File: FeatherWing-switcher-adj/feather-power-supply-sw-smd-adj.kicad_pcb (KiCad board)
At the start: 2 copper layers, 20 parts, among them J2 Conn_01x16, J3 QWIIC, J4 0.1, Q1 Q_PMOS_GSD, U1 MCP16312MS

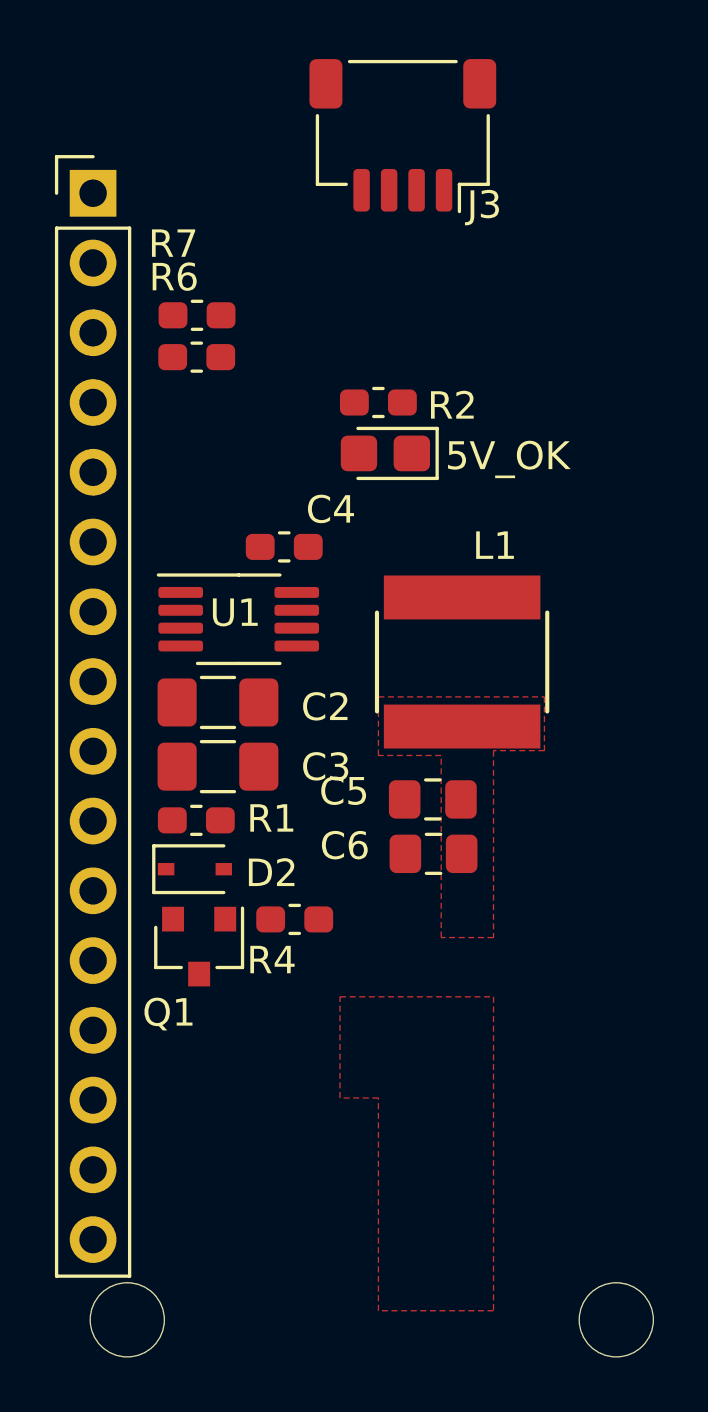
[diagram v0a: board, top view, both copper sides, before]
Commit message: adds input switch
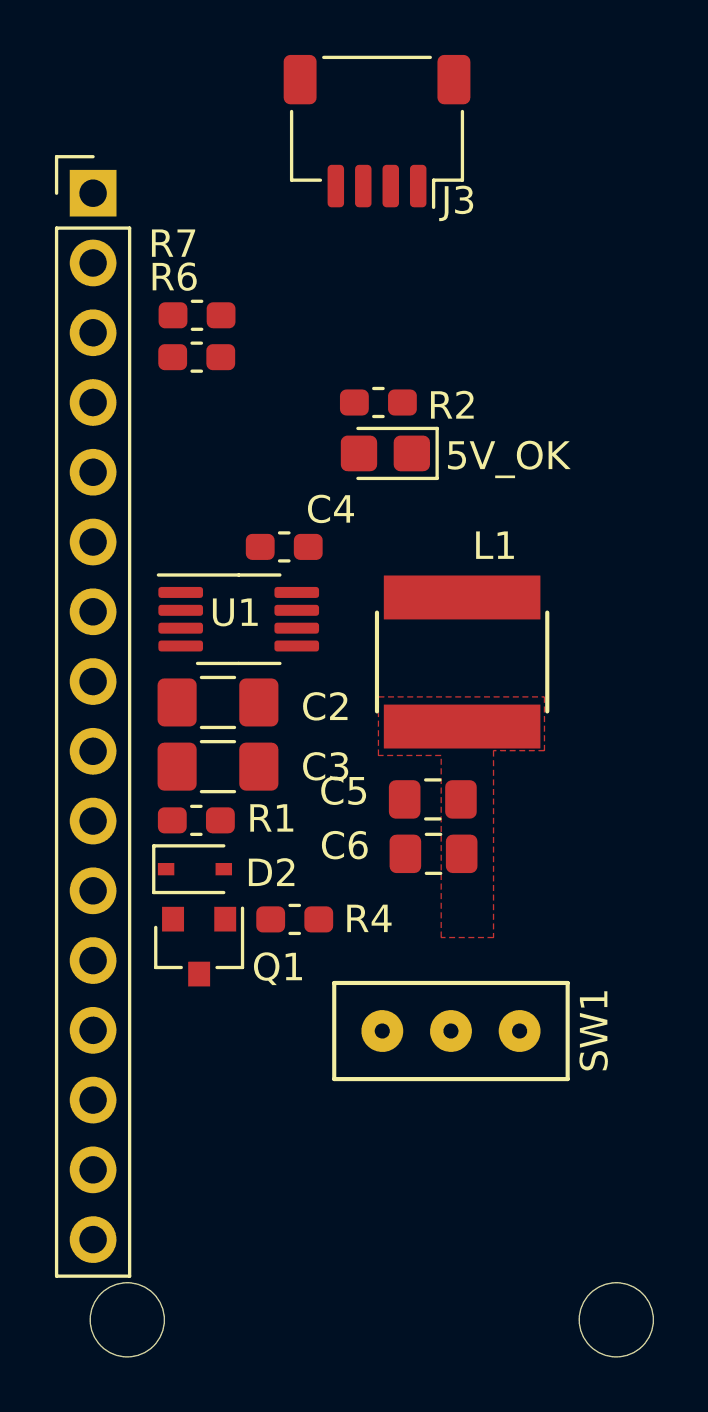
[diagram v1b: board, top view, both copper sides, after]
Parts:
- added SW1: SW_SPDT, My libs:sw-spdt-DIYhz, F.Cu at (142.6, 96.5)
- moved J3 0.95 mm to (139.9, 63.7)
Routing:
- removed copper zone on F.Cu, net VCC

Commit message: adds led jp
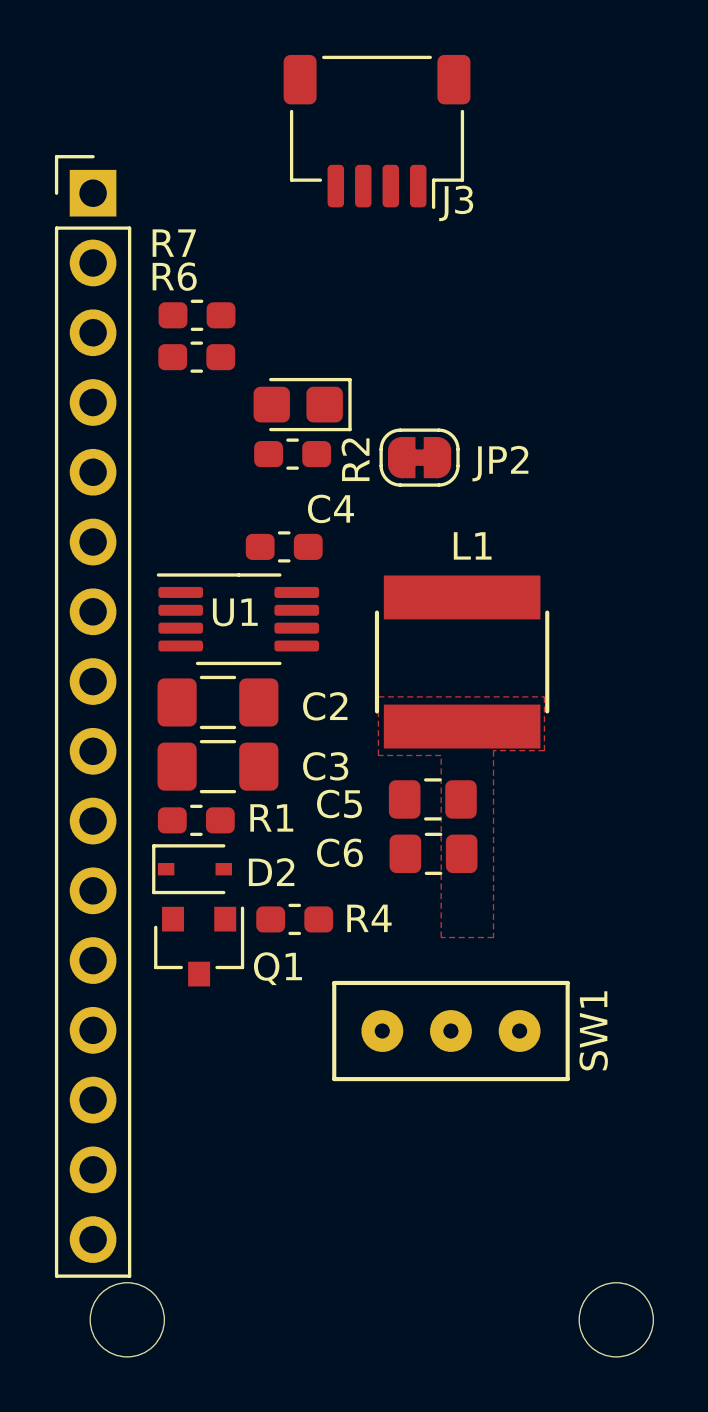
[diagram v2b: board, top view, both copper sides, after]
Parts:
- added JP2: SolderJumper_2_Bridged, Jumper:SolderJumper-2_P1.3mm_Bridged_RoundedPad1.0x1.5mm, F.Cu at (141.5, 75.6)
- D3: value 5V_OK -> +5V
- moved R2 3.65 mm to (136.8, 75.5)
- moved D3 3.64 mm to (137.0, 73.7)
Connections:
- R2 pad 1: +5V -> Net-(JP2-Pad2)
